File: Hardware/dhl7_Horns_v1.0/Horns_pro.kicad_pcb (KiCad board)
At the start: 2 copper layers, 31 x 33 mm, 19 parts, among them J1 Power, J2 Horn Control, J3 Horn Out, J4 Horn Out, Q1 Q_NMOS_DGS

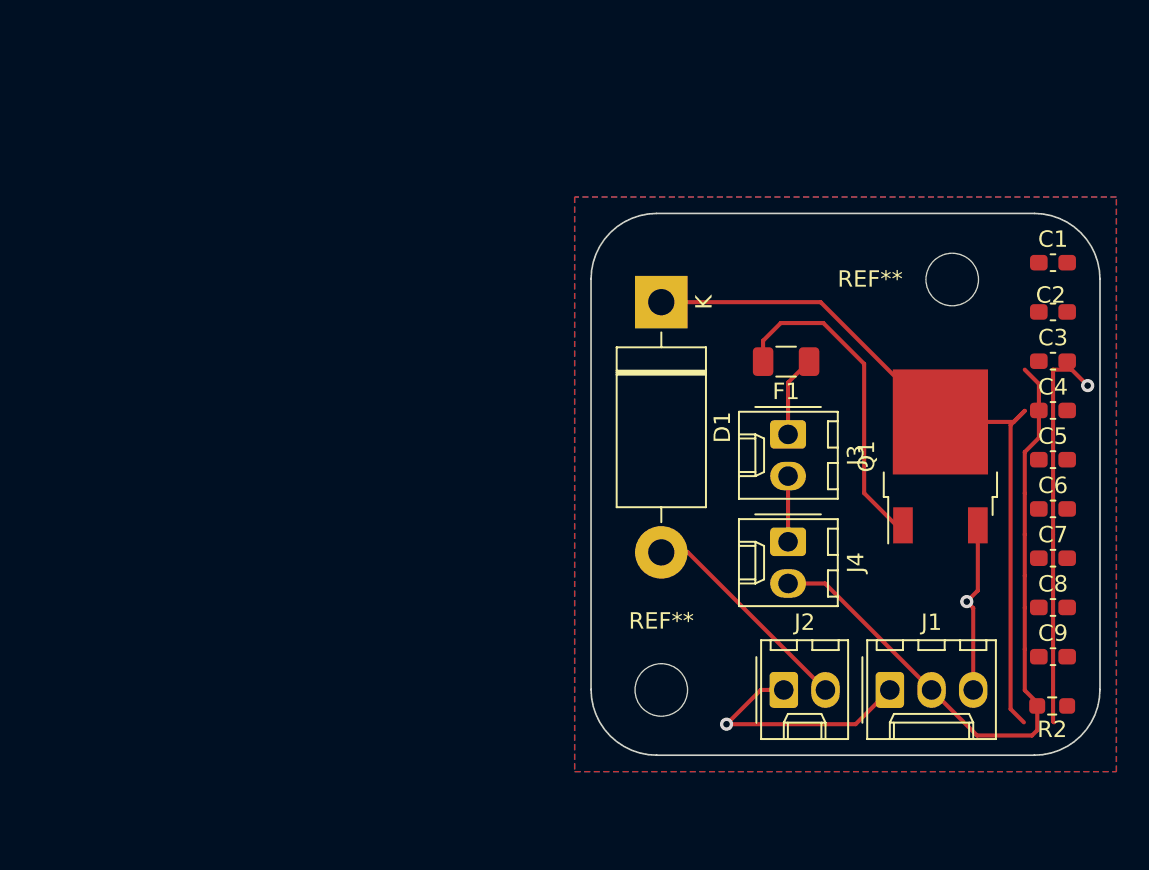
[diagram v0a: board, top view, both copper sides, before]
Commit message: didnt do the gerber thingy bc no directions as tutorial is broken
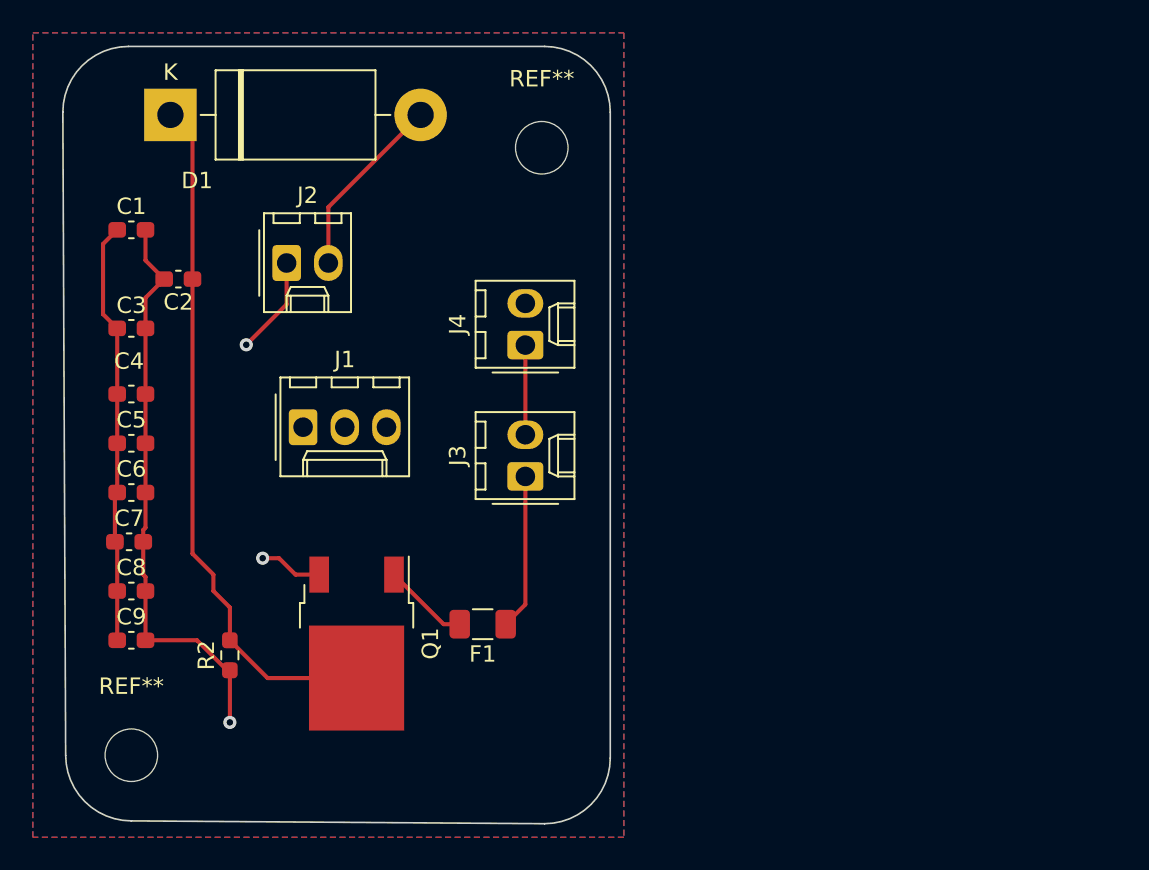
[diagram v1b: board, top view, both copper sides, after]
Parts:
- removed the REF** at (123.3, 97.0)
- removed the REF** at (141.0, 72.0)
- added REF**: MountingHole_3.2mm_M3, MountingHole:MountingHole_3.2mm_M3, F.Cu at (91.0, 101.0)
- added REF**: MountingHole_3.2mm_M3, MountingHole:MountingHole_3.2mm_M3, F.Cu at (116.0, 64.0)
- moved C7 56.3 mm to (90.9, 88.0)
- moved C1 56.2 mm to (91.0, 69.0)
- moved C3 56.2 mm to (91.0, 75.0)
- moved C4 56.1 mm to (91.0, 79.0)
- moved C5 56.1 mm to (91.0, 82.0)
- moved C6 56.1 mm to (91.0, 85.0)
- moved C8 56.1 mm to (91.0, 91.0)
- moved C9 56.1 mm to (91.0, 94.0)
- moved C2 53.3 mm to (93.9, 72.0), turned to 0 degrees
- moved R2 50.2 mm to (97.0, 94.9), turned to 90 degrees
- moved J2 39.9 mm to (100.5, 71.0)
- moved J1 39.2 mm to (101.5, 81.0)
- moved Q1 37.3 mm to (104.7, 94.2), turned to -90 degrees
- moved D1 32.0 mm to (93.4, 62.0), turned to 0 degrees
- moved F1 24.4 mm to (112.4, 93.0)
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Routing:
- net Net-(Q1-D): track 21.7 -> 5.25 mm
- net +24V: track 42.1 -> 25.8 mm
- net GND: track 49.6 -> 45.1 mm
- net Net-(J3-Pin_1): track 4.97 -> 9.50 mm
- net Net-(D1-K): track 45.1 -> 42.2 mm
- net /Horn input: track 13.5 -> 11.3 mm
- net Net-(J3-Pin_2): track 4.00 -> 5.46 mm
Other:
- board size 31 x 33 mm -> 33.3 x 47.3 mm
